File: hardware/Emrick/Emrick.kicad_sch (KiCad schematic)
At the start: 90 parts, among them J1 LED_STRIP_CONNECTOR, J3 Conn_02x05_Odd_Even, J4 BATT_CONN, P1 USB_C_Plug_USB2.0, Q1 Q_NMOS_GSD, Q2 Q_NMOS_GSD, Q3 Q_NMOS_GSD, SW1 SW_SPST, U1 74HCT541, U2 CC1310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

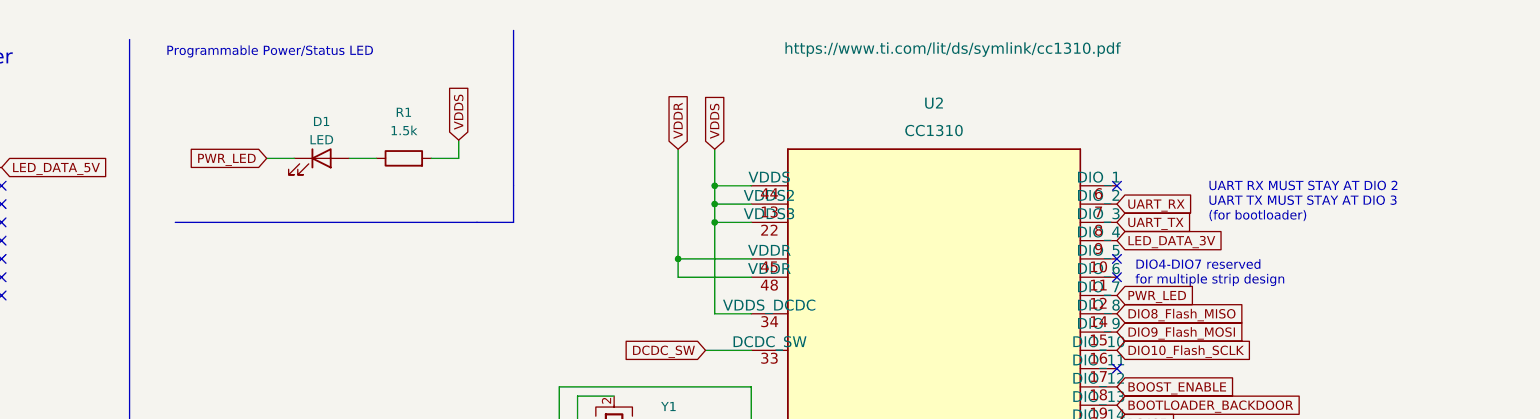
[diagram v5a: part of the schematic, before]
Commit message: Revision 5.1
- Switch to vertical smaller batter switch
- Add LED power button that is connected to the cc1310
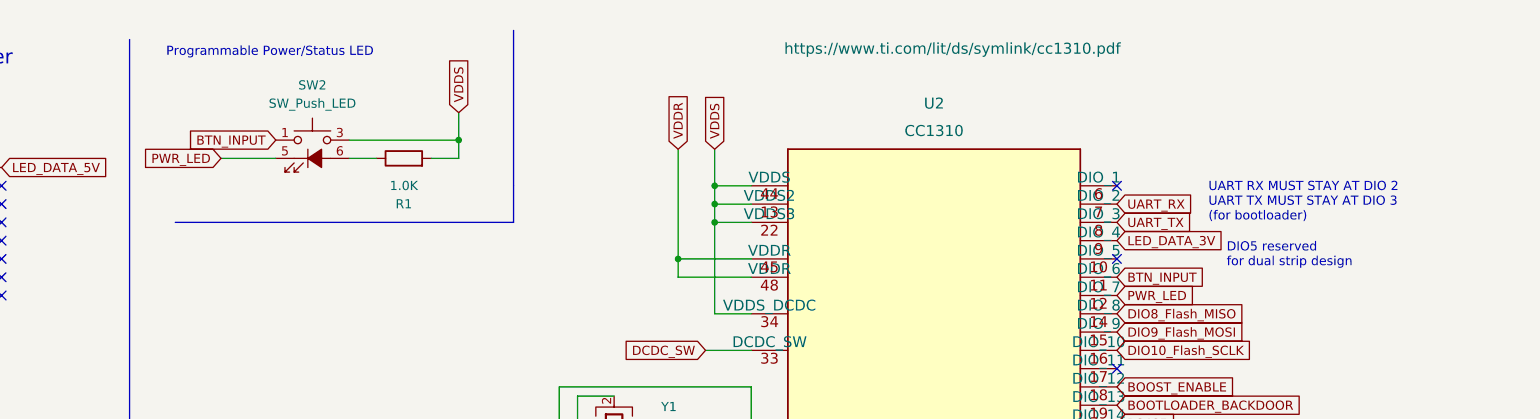
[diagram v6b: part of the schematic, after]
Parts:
- removed D1: LED, LED_SMD:LED_0402_1005Metric, symbol Device:LED
- added SW2: SW_Push_LED, footprints.pretty:SW-SMD_CHA_C603B-101ML-1SF, symbol Switch:SW_Push_LED
- R1: value 1.5k -> 1.0K
- SW1: footprint xkbconnectivity:SW-TH_SS-12D11G4R -> footprints.pretty:SW-TH_SS-12F45-GXXX
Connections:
- net PWR_LED: now also SW2.5 (K)
- net VDDS: now also SW2.3
- net BTN_INPUT: now reaches U2.11 (DIO_6)
- net BTN_INPUT: now also SW2.1
- net at R1.1: now also SW2.6 (A)
- no-connect marks 30 -> 29
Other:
- note added: "DIO5 reserved for dual strip design"
- note removed: "DIO4-DIO7 reserved for multiple strip design"
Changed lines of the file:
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@@
     (title "Project Emrick Light Strip")
     (date "2022-10-10")
-    (rev "5")
+    (rev "5.1")
   )
   (junction (at 36.83 43.18) (diameter 0) (color 0 0 0 0)
@@
   (junction (at 377.19 220.98) (diameter 0) (color 0 0 0 0)
   )
+  (junction (at 125.73 31.75) (diameter 0) (color 0 0 0 0)
+  )
   (junction (at 377.19 213.36) (diameter 0) (color 0 0 0 0)
   )
@@
   (no_connect (at 217.17 38.1))
   (no_connect (at 217.17 48.26))
-  (no_connect (at 217.17 50.8))
   (no_connect (at 62.23 45.72))
   (no_connect (at 62.23 48.26))
@@
     (stroke (width 0) (type default))
   )
-  (wire (pts (xy 99.06 34.29) (xy 102.87 34.29))
-    (stroke (width 0) (type default))
-  )
   (wire (pts (xy 359.41 71.12) (xy 367.03 71.12))
     (stroke (width 0) (type default))
@@
     (stroke (width 0) (type default))
   )
+  (wire (pts (xy 125.73 31.75) (xy 110.49 31.75))
+    (stroke (width 0) (type default))
+  )
   (wire (pts (xy 156.21 33.02) (xy 156.21 48.26))
     (stroke (width 0) (type default))
@@
     (stroke (width 0) (type default))
   )
+  (wire (pts (xy 92.71 34.29) (xy 100.33 34.29))
+    (stroke (width 0) (type default))
+  )
   (wire (pts (xy 50.8 177.8) (xy 45.72 177.8))
     (stroke (width 0) (type default))
@@
     (stroke (width 0) (type default))
   )
-  (wire (pts (xy 110.49 34.29) (xy 114.3 34.29))
-    (stroke (width 0) (type default))
-  )
   (wire (pts (xy 264.16 255.27) (xy 280.67 255.27))
     (stroke (width 0) (type default))
@@
     (stroke (width 0) (type default))
   )
+  (wire (pts (xy 125.73 31.75) (xy 125.73 34.29))
+    (stroke (width 0) (type default))
+  )
   (wire (pts (xy 59.69 140.97) (xy 62.23 140.97))
     (stroke (width 0) (type default))
@@
     (stroke (width 0) (type default))
   )
-  (wire (pts (xy 125.73 31.75) (xy 125.73 34.29))
+  (wire (pts (xy 125.73 27.94) (xy 125.73 31.75))
     (stroke (width 0) (type default))
   )
@@
     (stroke (width 0) (type default))
   )
+  (wire (pts (xy 110.49 34.29) (xy 114.3 34.29))
+    (stroke (width 0) (type default))
+  )
   (wire (pts (xy 153.67 269.24) (xy 151.13 269.24))
     (stroke (width 0) (type default))
@@
     (effects (font (size 2 2)) (justify left bottom))
   )
-  (text "DIO4-DIO7 reserved\nfor multiple strip design" (at 219.71 52.07 0)
+  (text "DIO5 reserved\nfor dual strip design" (at 232.41 49.53 0)
     (effects (font (size 1.27 1.27)) (justify left bottom))
   )
@@
     )
   )
+  (global_label "BTN_INPUT" (shape input) (at 217.17 50.8 0) (fields_autoplaced)
+    (effects (font (size 1.27 1.27)) (justify left))
+    (property "Intersheetrefs" "${INTERSHEET_REFS}" (at 230.1149 50.8 0)
+      (effects (font (size 1.27 1.27)) (justify left) hide)
+    )
+  )
   (global_label "UART_TX" (shape input) (at 93.98 250.19 0) (fields_autoplaced)
     (effects (font (size 1.27 1.27)) (justify left))
@@
     )
   )
-  (global_label "PWR_LED" (shape input) (at 99.06 34.29 180) (fields_autoplaced)
+  (global_label "PWR_LED" (shape input) (at 92.71 34.29 180) (fields_autoplaced)
     (effects (font (size 1.27 1.27)) (justify right))
-    (property "Intersheetrefs" "${INTERSHEET_REFS}" (at 88.2407 34.3694 0)
+    (property "Intersheetrefs" "${INTERSHEET_REFS}" (at 81.8907 34.3694 0)
       (effects (font (size 1.27 1.27)) (justify right) hide)
     )
@@
     )
   )
-  (global_label "VDDS" (shape input) (at 125.73 31.75 90) (fields_autoplaced)
+  (global_label "VDDS" (shape input) (at 125.73 27.94 90) (fields_autoplaced)
     (effects (font (size 1.27 1.27)) (justify left))
-    (property "Intersheetrefs" "${INTERSHEET_REFS}" (at 125.6506 24.4988 90)
+    (property "Intersheetrefs" "${INTERSHEET_REFS}" (at 125.6506 20.6888 90)
       (effects (font (size 1.27 1.27)) (justify left) hide)
     )
@@
     )
   )
+  (global_label "BTN_INPUT" (shape input) (at 100.33 31.75 180) (fields_autoplaced)
+    (effects (font (size 1.27 1.27)) (justify right))
+    (property "Intersheetrefs" "${INTERSHEET_REFS}" (at 87.3851 31.75 0)
+      (effects (font (size 1.27 1.27)) (justify right) hide)
+    )
+  )
   (global_label "BAT_CHG" (shape input) (at 217.17 96.52 0) (fields_autoplaced)
     (effects (font (size 1.27 1.27)) (justify left))
@@
       (effects (font (size 1.27 1.27)))
     )
-    (property "Footprint" "xkbconnectivity:SW-TH_SS-12D11G4R" (at 110.49 182.88 0)
+    (property "Footprint" "footprints.pretty:SW-TH_SS-12F45-GXXX" (at 110.49 182.88 0)
       (effects (font (size 1.27 1.27)) hide)
     )
@@
   )
   (symbol (lib_id "Device:R") (at 118.11 34.29 90) (unit 1)
-    (in_bom yes) (on_board yes) (dnp no) (fields_autoplaced)
-    (property "Reference" "R1" (at 118.11 27.94 90)
+    (in_bom yes) (on_board yes) (dnp no)
+    (property "Reference" "R1" (at 118.11 40.64 90)
       (effects (font (size 1.27 1.27)))
     )
-    (property "Value" "1.5k" (at 118.11 30.48 90)
+    (property "Value" "1.0K" (at 118.11 38.1 90)
       (effects (font (size 1.27 1.27)))
     )
@@
     (pin "A4")
     (pin "A5")
-    (pin "B6")
     (pin "A6")
     (pin "A7")
-    (pin "B7")
     (pin "A9")
     (pin "B1")
@@
     (pin "B4")
     (pin "B5")
+    (pin "B6")
+    (pin "B7")
     (pin "B9")
     (pin "S1")
@@
     )
   )
+  (symbol (lib_id "Switch:SW_Push_LED") (at 105.41 34.29 0) (unit 1)
+    (in_bom yes) (on_board yes) (dnp no)
+    (property "Reference" "SW2" (at 105.41 24.13 0)
+      (effects (font (size 1.27 1.27)))
+    )
+    (property "Value" "SW_Push_LED" (at 105.41 26.67 0)
+      (effects (font (size 1.27 1.27)))
+    )
+    (property "Footprint" "footprints.pretty:SW-SMD_CHA_C603B-101ML-1SF" (at 105.41 41.91 0)
+      (effects (font (size 1.27 1.27)) hide)
+    )
+    (property "Datasheet" "~" (at 105.41 41.91 0)
+      (effects (font (size 1.27 1.27)) hide)
+    )
+    (pin "1")
+    (pin "3")
+    (pin "5")
+    (pin "6")
+    (instances
+      (project "Emrick"
+        (path "/3273eadb-35bb-41d4-911c-7b885ba92916"
+          (reference "SW2") (unit 1)
+        )
+      )
+    )
+  )
   (symbol (lib_id "Device:C") (at 246.38 121.92 90) (unit 1)
     (in_bom yes) (on_board yes) (dnp no)
@@
         )
       )
-    )
-  )
-  (symbol (lib_id "Device:LED") (at 106.68 34.29 0) (unit 1)
-    (in_bom yes) (on_board yes) (dnp no)
-    (property "Reference" "D1" (at 106.68 29.21 0)
-      (effects (font (size 1.27 1.27)))
-    )
-    (property "Value" "LED" (at 106.68 31.75 0)
-      (effects (font (size 1.27 1.27)))
-    )
-    (property "Footprint" "LED_SMD:LED_0402_1005Metric" (at 106.68 34.29 0)
-      (effects (font (size 1.27 1.27)) hide)
-    )
-    (property "Datasheet" "~" (at 106.68 34.29 0)
-      (effects (font (size 1.27 1.27)) hide)
-    )
-    (pin "1")
-    (pin "2")
-    (instances
-      (project "Emrick"
-        (path "/3273eadb-35bb-41d4-911c-7b885ba92916"
-          (reference "D1") (unit 1)
-        )
-      )

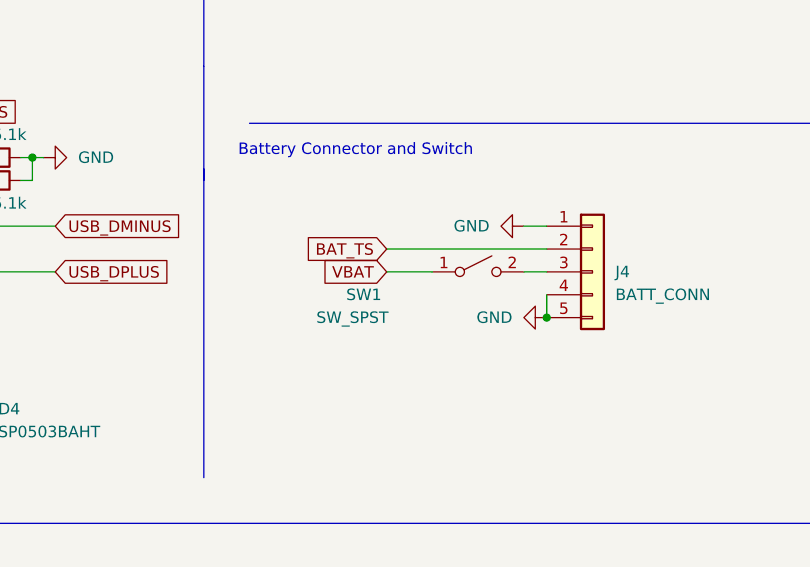
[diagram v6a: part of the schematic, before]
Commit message: Replaced SW1
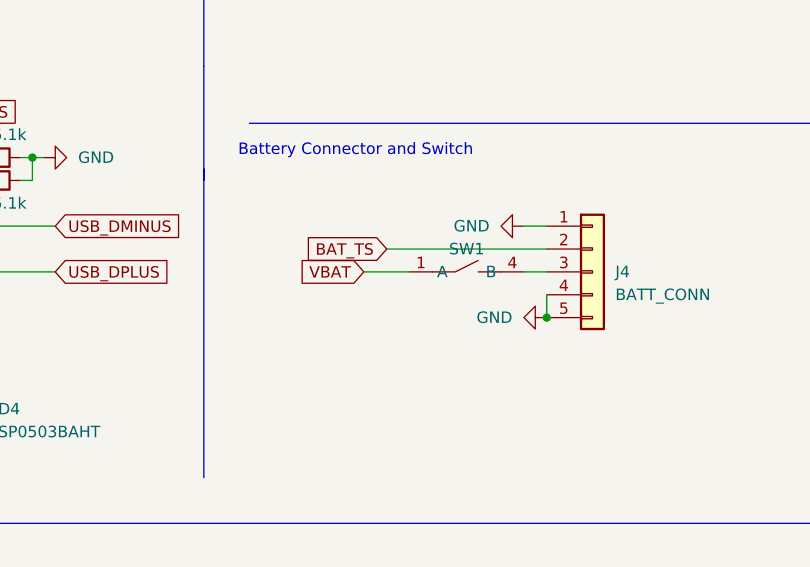
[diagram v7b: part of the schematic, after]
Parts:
- removed SW1: SW_SPST, footprints.pretty:SW-TH_SS-12F45-GXXX, symbol Switch:SW_SPST
- added SW1: ~, custom_components:MST22D18G2_125, symbol custom_componentsFull:MST22D18G2_125
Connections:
- net VBAT: now also SW1.1 (A)
- net at J4.3 (Pin_3): now also SW1.4 (B)
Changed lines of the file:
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@@
     (stroke (width 0) (type default))
   )
-  (wire (pts (xy 100.33 182.88) (xy 105.41 182.88))
+  (wire (pts (xy 97.79 182.88) (xy 102.87 182.88))
     (stroke (width 0) (type default))
   )
@@
     )
   )
-  (global_label "VBAT" (shape input) (at 100.33 182.88 180) (fields_autoplaced)
+  (global_label "VBAT" (shape input) (at 97.79 182.88 180) (fields_autoplaced)
     (effects (font (size 1.27 1.27)) (justify right))
-    (property "Intersheetrefs" "${INTERSHEET_REFS}" (at 93.0094 182.88 0)
+    (property "Intersheetrefs" "${INTERSHEET_REFS}" (at 90.4694 182.88 0)
       (effects (font (size 1.27 1.27)) (justify right) hide)
     )
@@
     )
   )
-  (symbol (lib_id "Switch:SW_SPST") (at 110.49 182.88 0) (unit 1)
-    (in_bom yes) (on_board yes) (dnp no)
-    (property "Reference" "SW1" (at 97.79 185.42 0)
-      (effects (font (size 1.27 1.27)))
-    )
-    (property "Value" "SW_SPST" (at 96.52 187.96 0)
-      (effects (font (size 1.27 1.27)))
-    )
-    (property "Footprint" "footprints.pretty:SW-TH_SS-12F45-GXXX" (at 110.49 182.88 0)
-      (effects (font (size 1.27 1.27)) hide)
-    )
-    (property "Datasheet" "~" (at 110.49 182.88 0)
-      (effects (font (size 1.27 1.27)) hide)
-    )
-    (pin "1")
-    (pin "2")
-    (instances
-      (project "Emrick"
-        (path "/3273eadb-35bb-41d4-911c-7b885ba92916"
-          (reference "SW1") (unit 1)
-        )
-      )
-    )
-  )
   (symbol (lib_id "power:GND") (at 41.91 101.6 270) (unit 1)
     (in_bom yes) (on_board yes) (dnp no) (fields_autoplaced)
@@
         )
       )
+    )
+  )
+  (symbol (lib_id "custom_componentsFull:MST22D18G2_125") (at 109.22 180.34 0) (unit 1)
+    (in_bom yes) (on_board yes) (dnp no) (fields_autoplaced)
+    (property "Reference" "SW1" (at 109.22 180.34 0)
+      (effects (font (size 1.27 1.27)))
+    )
+    (property "Value" "~" (at 109.22 180.34 0)
+      (effects (font (size 1.27 1.27)))
+    )
+    (property "Footprint" "custom_components:MST22D18G2_125" (at 109.22 180.34 0)
+      (effects (font (size 1.27 1.27)) hide)
+    )
+    (property "Datasheet" "" (at 109.22 180.34 0)
+      (effects (font (size 1.27 1.27)) hide)
+    )
+    (pin "1")
+    (pin "4")
+    (instances
+      (project "Emrick"
+        (path "/3273eadb-35bb-41d4-911c-7b885ba92916"
+          (reference "SW1") (unit 1)
+        )
+      )

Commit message: Reverted to old switch (SW1)
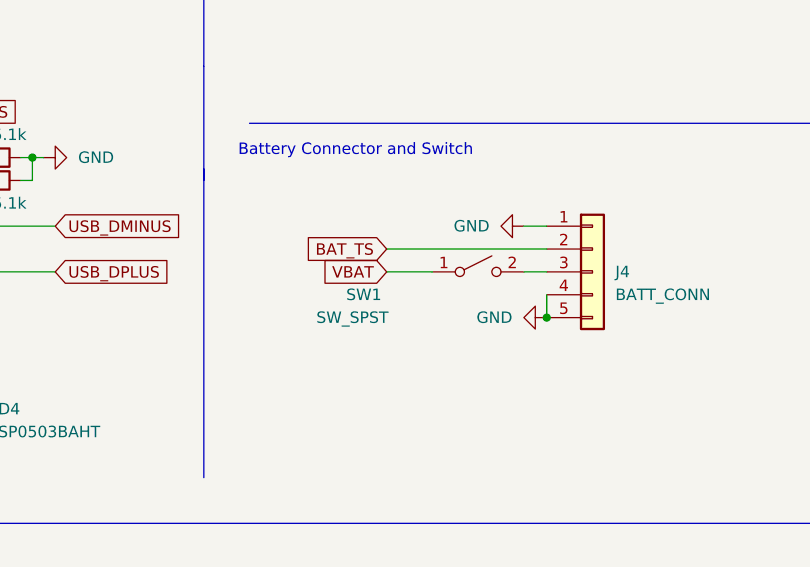
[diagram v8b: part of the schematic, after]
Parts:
- removed SW1: ~, custom_components:MST22D18G2_125, symbol custom_componentsFull:MST22D18G2_125
- added SW1: SW_SPST, switch_original:SW-TH_SS-12F45-GXXX, symbol Switch:SW_SPST
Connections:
- net VBAT: now also SW1.1 (A)
- net at J4.3 (Pin_3): now also SW1.2 (B)
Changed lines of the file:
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@@
     (stroke (width 0) (type default))
   )
-  (wire (pts (xy 97.79 182.88) (xy 102.87 182.88))
+  (wire (pts (xy 100.33 182.88) (xy 105.41 182.88))
     (stroke (width 0) (type default))
   )
@@
     )
   )
-  (global_label "VBAT" (shape input) (at 97.79 182.88 180) (fields_autoplaced)
+  (global_label "VBAT" (shape input) (at 100.33 182.88 180) (fields_autoplaced)
     (effects (font (size 1.27 1.27)) (justify right))
-    (property "Intersheetrefs" "${INTERSHEET_REFS}" (at 90.4694 182.88 0)
+    (property "Intersheetrefs" "${INTERSHEET_REFS}" (at 93.0094 182.88 0)
       (effects (font (size 1.27 1.27)) (justify right) hide)
     )
@@
     )
   )
+  (symbol (lib_id "Switch:SW_SPST") (at 110.49 182.88 0) (unit 1)
+    (in_bom yes) (on_board yes) (dnp no)
+    (property "Reference" "SW1" (at 97.79 185.42 0)
+      (effects (font (size 1.27 1.27)))
+    )
+    (property "Value" "SW_SPST" (at 96.52 187.96 0)
+      (effects (font (size 1.27 1.27)))
+    )
+    (property "Footprint" "switch_original:SW-TH_SS-12F45-GXXX" (at 110.49 182.88 0)
+      (effects (font (size 1.27 1.27)) hide)
+    )
+    (property "Datasheet" "~" (at 110.49 182.88 0)
+      (effects (font (size 1.27 1.27)) hide)
+    )
+    (pin "1")
+    (pin "2")
+    (instances
+      (project "Emrick"
+        (path "/3273eadb-35bb-41d4-911c-7b885ba92916"
+          (reference "SW1") (unit 1)
+        )
+      )
+    )
+  )
   (symbol (lib_id "Device:FerriteBead") (at 336.55 36.83 90) (unit 1)
     (in_bom yes) (on_board yes) (dnp no)
@@
         )
       )
-    )
-  )
-  (symbol (lib_id "custom_componentsFull:MST22D18G2_125") (at 109.22 180.34 0) (unit 1)
-    (in_bom yes) (on_board yes) (dnp no) (fields_autoplaced)
-    (property "Reference" "SW1" (at 109.22 180.34 0)
-      (effects (font (size 1.27 1.27)))
-    )
-    (property "Value" "~" (at 109.22 180.34 0)
-      (effects (font (size 1.27 1.27)))
-    )
-    (property "Footprint" "custom_components:MST22D18G2_125" (at 109.22 180.34 0)
-      (effects (font (size 1.27 1.27)) hide)
-    )
-    (property "Datasheet" "" (at 109.22 180.34 0)
-      (effects (font (size 1.27 1.27)) hide)
-    )
-    (pin "1")
-    (pin "4")
-    (instances
-      (project "Emrick"
-        (path "/3273eadb-35bb-41d4-911c-7b885ba92916"
-          (reference "SW1") (unit 1)
-        )
-      )
